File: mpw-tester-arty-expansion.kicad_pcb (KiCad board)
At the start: 4 copper layers, 53.3 x 61.5 mm, 138 parts, among them J1 USB4105-GF-A, J10 61300211121, J11 61300211121, J12 61300211121, J13 61300211121, J14 61300211121, J15 61300211121, J16 61300211121, J17 61300211121, J18 61300411121, J19 61300711121, J2 61300211121, J20 61300411121, J3 Arty_A7_SPI, J4 61300211121, J5 61300311121, J6 61300211121, J7 61300211121, J8 61300211121, J9 61300211121, Q1 DTC014TEBTL, U1 SN74LVC1G125DCKR, U2 FT232HQ, U3 SN74LVC1G125DCKR, U4 MAX811REUS+T, U5 NTS0102GT, U6 MCP4661-103E/ML, U7 Caravel_breakout_PCB, U8 W25Q32FVSS, U9 MIC2211-AAYML-TR, Y1 ABM8G-12.000MHZ-18-D2Y-T, Y2 ECS-2520MVLC-100-BN-TR

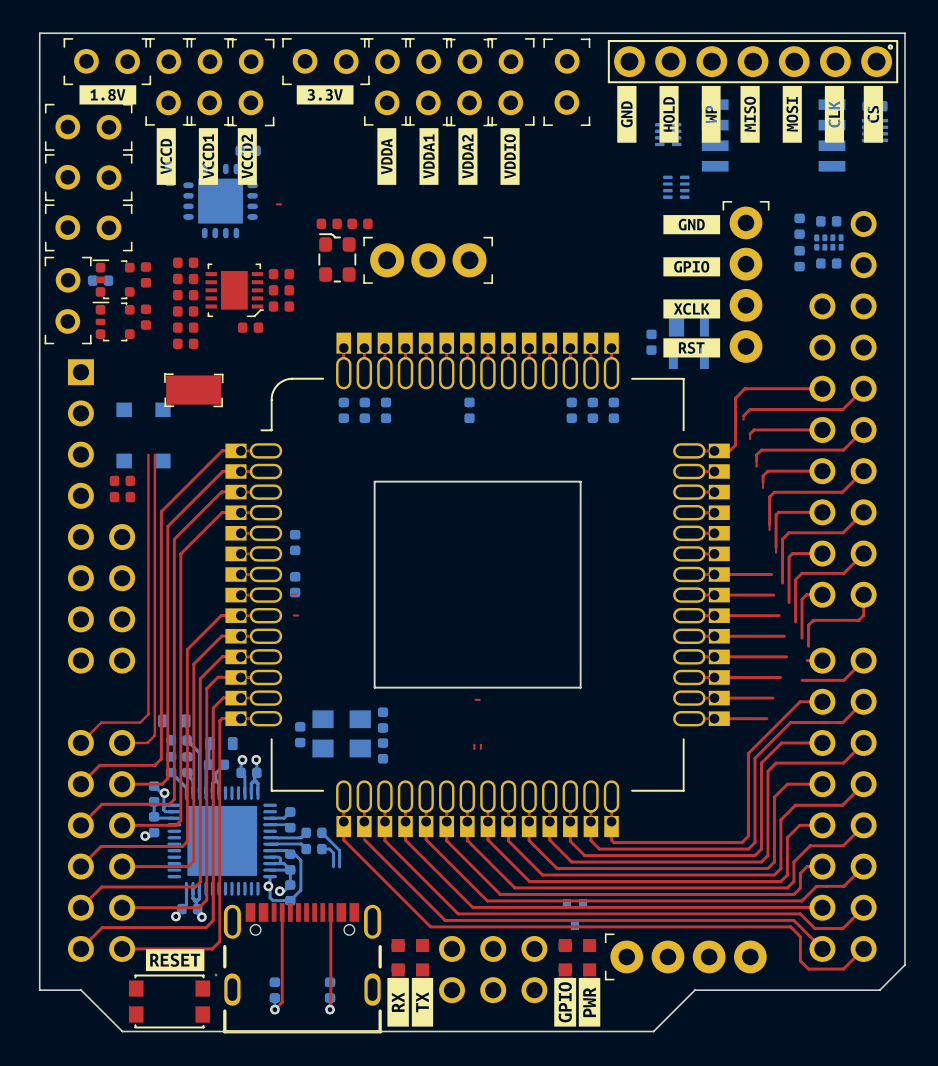
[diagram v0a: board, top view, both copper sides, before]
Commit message: Import changes to PCB, adjust placement
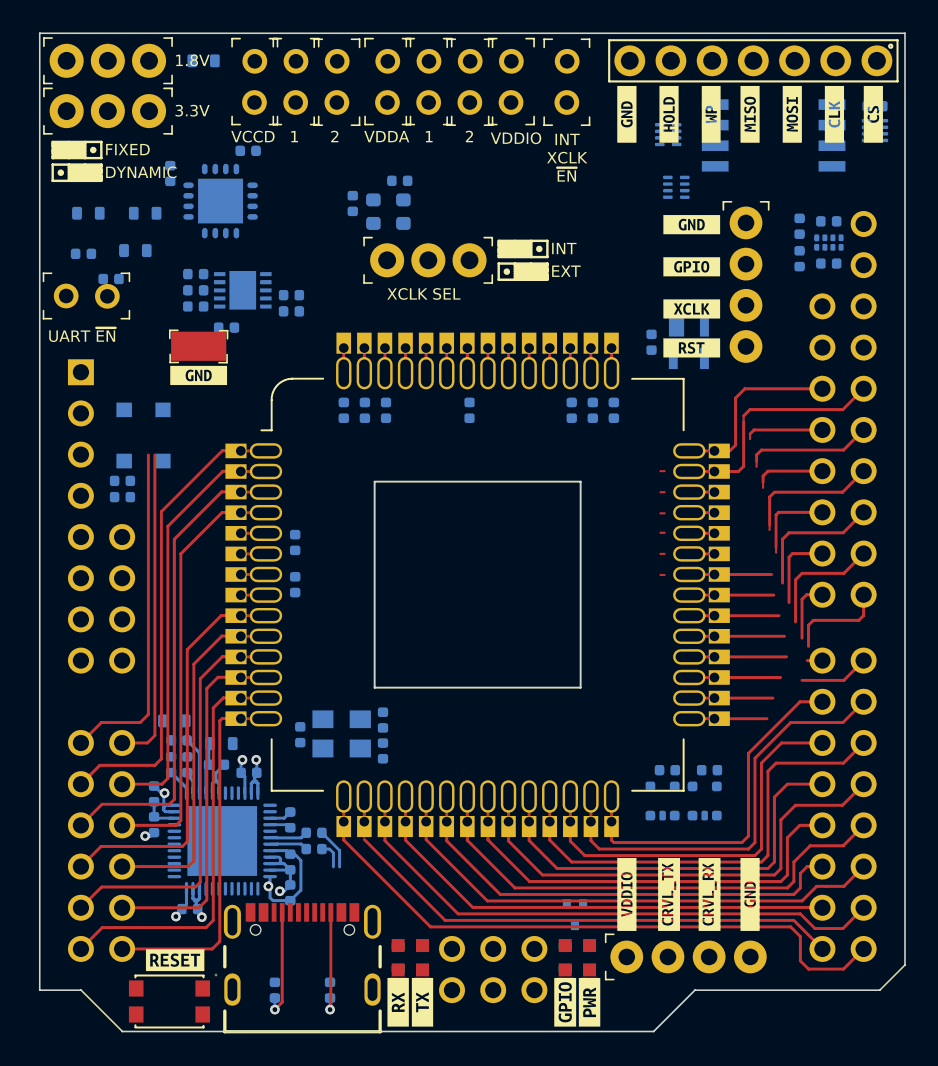
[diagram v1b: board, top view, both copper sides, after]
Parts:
- removed J13, J16, J17: 61300211121, antmicro-footprints:PinHeader_1x2_P2.54_Drill0.9mm
- removed kibuzzard-638FA122: G***, kibuzzard-638FA122
- removed kibuzzard-638FA139: G***, kibuzzard-638FA139
- removed kibuzzard-638FA13E: G***, kibuzzard-638FA13E
- removed kibuzzard-638FA141: G***, kibuzzard-638FA141
- removed kibuzzard-638FA14D: G***, kibuzzard-638FA14D
- removed kibuzzard-638FA15A: G***, kibuzzard-638FA15A
- removed kibuzzard-638FA169: G***, kibuzzard-638FA169
- removed kibuzzard-638FA16F: G***, kibuzzard-638FA16F
- removed kibuzzard-638FA174: G***, kibuzzard-638FA174
- added R26: R_10k_0603, antmicro-footprints:0603-res, B.Cu at (133.1, 67.7)
- added kibuzzard-638FA1CB: G***, kibuzzard-638FA1CB, F.Cu at (132.8, 87.1)
- added kibuzzard-639040B1: G***, kibuzzard-639040B1, F.Cu at (164.3, 119.1)
- added kibuzzard-639040B6: G***, kibuzzard-639040B6, F.Cu at (161.8, 119.1)
- added kibuzzard-639040BB: G***, kibuzzard-639040BB, F.Cu at (159.2, 119.1)
- added kibuzzard-639040CA: G***, kibuzzard-639040CA, F.Cu at (166.8, 119.1)
- C10, C18, C19, C3, C32, C33, C35, C36, C4, R11, R17, R21, U1, U3, U9, Y2: moved to B.Cu
- J14, J15: value 61300211121 -> 61300311121; footprint antmicro-footprints:PinHeader_1x2_P2.54_Drill0.9mm -> antmicro-footprints:PinHeader_1x3_P2.54_Drill1.1mm
- R22: value R_10k_0402 -> R_68k_0603; footprint antmicro-footprints:0402-res -> antmicro-footprints:0603-res; moved to B.Cu
- R23: value R_10k_0402 -> R_41k2_0603; footprint antmicro-footprints:0402-res -> antmicro-footprints:0603-res; moved to B.Cu
- R24: value R_10k_0402 -> R_15k_0603; footprint antmicro-footprints:0402-res -> antmicro-footprints:0603-res; moved to B.Cu
- R25: value R_10k_0402 -> R_34k_0402; moved to B.Cu
- moved U1 48.5 mm to (164.0, 113.3), turned to 180 degrees
- moved C10 46.3 mm to (164.3, 111.4), turned to 180 degrees
- moved U3 44.9 mm to (161.4, 113.3), turned to 180 degrees
- moved C18 42.6 mm to (161.7, 111.4), turned to 180 degrees
- moved NT9 28.8 mm to (161.4, 93.0), turned to 180 degrees
- moved NT11 22.9 mm to (161.4, 98.1), turned to 180 degrees
- moved NT12 22.7 mm to (161.4, 99.4), turned to 180 degrees
- moved NT8 19.5 mm to (161.4, 94.3), turned to 180 degrees
- moved NT7 17.3 mm to (161.4, 96.8), turned to 180 degrees
- moved NT10 16.2 mm to (161.4, 95.6), turned to 180 degrees
- moved J15 10.6 mm to (124.7, 67.7), turned to 0 degrees
- moved R25 8.40 mm to (125.7, 79.6)
- moved R23 6.73 mm to (126.0, 77.1)
- moved C35 6.52 mm to (138.5, 83.2), turned to 0 degrees
- moved C36 6.52 mm to (138.5, 82.2), turned to 0 degrees
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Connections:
- net /ADJ1 renamed /P0W
- net /ADJ2 renamed /P1W
- C23 pad 1: /5V0_SEL -> /5V0
- C32 pad 1: /5V0_SEL -> /5V0
- C35 pad 1: /VOUT1 -> +3V3
- C36 pad 1: /VOUT2 -> +1V8
- J14 pad 1: /P1A -> /P0B
- J14 pad 2: /P1B -> /P0A
- J15 pad 1: /P0A -> /P1B
- J15 pad 2: /P0B -> /P1A
- R14 pad 2: /5V0_SEL -> /5V0
- R15 pad 1: /5V0_SEL -> /5V0
- R17 pad 1: /5V0_SEL -> /5V0
- R19 pad 1: /5V0_SEL -> /5V0
- R21 pad 1: /5V0_SEL -> /5V0
- R22 pad 1: /P1A -> /P0A
- R22 pad 2: /VOUT2 -> +3V3
- R23 pad 2: /P1B -> /P0B
- R24 pad 1: /P0A -> /P1A
- R24 pad 2: /VOUT1 -> +1V8
- R25 pad 2: /P0B -> /P1B
- U5 pad 7: /5V0_SEL -> /5V0
- U6 pad 15: /5V0_SEL -> /5V0
- U9 pad 1: /5V0_SEL -> /5V0
- U9 pad 10: /VOUT1 -> +3V3
- U9 pad 9: /VOUT2 -> +1V8
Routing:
- net /CRVL_IO1: track 1.55 -> 6.25 mm
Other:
- board text added: "1"
- board text added: "1.8V"
- board text added: "2"
- board text added: "3.3V"
- board text added: "DYNAMIC"
- board text added: "EXT"
- board text added: "FIXED"
- board text added: "INT"
- board text added: "INT XCLK ~{EN}"
- board text added: "UART ~{EN}"
- board text added: "VCCD"
- board text added: "VDDA"
- board text added: "VDDIO"
- board text added: "XCLK SEL"

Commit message: Import changes to PCB. Adjust placement. Partial layout
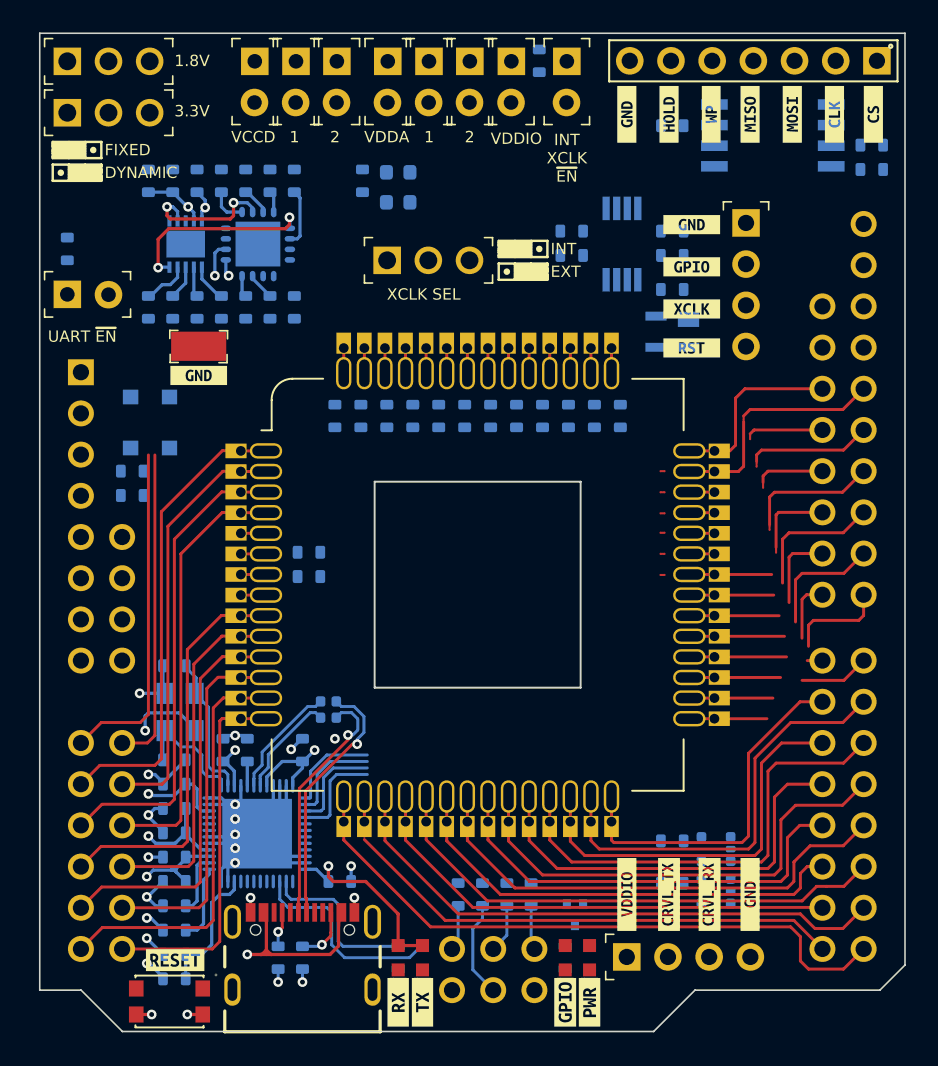
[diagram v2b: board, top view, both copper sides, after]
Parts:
- removed C13: C_100n_0402, antmicro-footprints:0402-cap
- added C37: C_100n_0603, antmicro-footprints:0603-cap, B.Cu at (137.2, 82.9)
- added R27: R_4k7_0603, antmicro-footprints:0603-res, B.Cu at (155.8, 78.2)
- added R28: R_10k_0603, antmicro-footprints:0603-res, B.Cu at (162.0, 71.7)
- added R29: R_0R_0603, antmicro-footprints:0603-res, B.Cu at (135.7, 82.9)
- added R30: R_10k_0603, antmicro-footprints:0603-res, B.Cu at (131.2, 82.9)
- added R31: R_4k7_0603, antmicro-footprints:0603-res, B.Cu at (155.8, 79.7)
- added R32: R_10k_0603, antmicro-footprints:0603-res, B.Cu at (174.3, 72.9)
- added R33: R_10k_0603, antmicro-footprints:0603-res, B.Cu at (132.7, 82.9)
- added R34: R_10k_0603, antmicro-footprints:0603-res, B.Cu at (146.0, 89.6)
- C1, C22, C23, C24, C26, C27, C28, C29, C30, C31: value C_100n_0402 -> C_1u_0603; footprint antmicro-footprints:0402-cap -> antmicro-footprints:0603-cap
- C10, C11, C14, C15, C16, C18, C19, C20, C21, C25, C33, C34, C5, C7, C8: value C_100n_0402 -> C_100n_0603; footprint antmicro-footprints:0402-cap -> antmicro-footprints:0603-cap
- C17: value C_10n_0402 -> C_10n_0603; footprint antmicro-footprints:0402-cap -> antmicro-footprints:0603-cap
- C3, C32, C35, C36: value C_1u_0402 -> C_1u_0603; footprint antmicro-footprints:0402-cap -> antmicro-footprints:0603-cap
- C4: value C_1u_0402 -> C_100n_0603; footprint antmicro-footprints:0402-cap -> antmicro-footprints:0603-cap
- C6, C9: value C_18p_0402 -> C_18p_0603; footprint antmicro-footprints:0402-cap -> antmicro-footprints:0603-cap
- R1, R17, R21, R6: value R_10k_0402 -> R_10k_0603; footprint antmicro-footprints:0402-res -> antmicro-footprints:0603-res
- R11, R14: value R_10k_0402 -> R_0R_0603; footprint antmicro-footprints:0402-res -> antmicro-footprints:0603-res
- R15: value R_4k7_0402 -> R_0R_0603; footprint antmicro-footprints:0402-res -> antmicro-footprints:0603-res
- R16, R20: value 4x10k_0201_array -> R_10k_0603; footprint antmicro-footprints:EXB18V -> antmicro-footprints:0603-res
- R18: value R_0R_0402 -> R_10k_0603; footprint antmicro-footprints:0402-res -> antmicro-footprints:0603-res
- R19: value R_4k7_0402 -> R_10k_0603; footprint antmicro-footprints:0402-res -> antmicro-footprints:0603-res
- R2, R3: value R_5k1_0402 -> R_5k1_0603; footprint antmicro-footprints:0402-res -> antmicro-footprints:0603-res
- R25: value R_34k_0402 -> R_34k_0603; footprint antmicro-footprints:0402-res -> antmicro-footprints:0603-res
- R7: value R_12k_0402 -> R_12k_1%_0603; footprint antmicro-footprints:0402-res -> antmicro-footprints:0603-res
- R8: value 4x0R_0201_array -> R_0R_0603; footprint antmicro-footprints:EXB18V -> antmicro-footprints:0603-res
- U5: value NTS0102GT -> NTS0102DP; footprint antmicro-footprints:PSON50P100X195X50-8N -> antmicro-footprints:TSSOP-8_W3mm
- moved R14 49.7 mm to (153.3, 119.1)
- moved R8 45.6 mm to (148.8, 119.1), turned to 90 degrees
- moved R15 45.6 mm to (150.3, 119.1), turned to 90 degrees
- moved R11 43.6 mm to (151.8, 119.1), turned to 90 degrees
- moved C23 28.8 mm to (144.4, 89.6), turned to -90 degrees
- moved R20 25.4 mm to (138.7, 82.9), turned to 90 degrees
- moved R18 24.4 mm to (154.0, 89.6), turned to 90 degrees
- moved C1 22.2 mm to (128.7, 94.5), turned to 0 degrees
- moved R19 21.4 mm to (150.8, 89.6)
- moved R16 21.1 mm to (153.8, 67.7), turned to -90 degrees
- moved R21 20.9 mm to (152.4, 89.6), turned to 90 degrees
- moved C4 18.0 mm to (131.3, 112.3), turned to 180 degrees
- moved R17 16.9 mm to (147.6, 89.6), turned to 90 degrees
- moved C24 14.5 mm to (158.8, 89.6)
- moved C9 13.3 mm to (131.3, 105.0), turned to 180 degrees
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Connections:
- net Net-(C33-Pad1) renamed /BYP
- C1 pad 1: /FTDI_3V3 -> /3V3_ARTY
- C23 pad 1: /5V0 -> /VDDA2
- C24 pad 1: /VDDA2 -> /VCCD1
- C25 pad 1: /VCCD1 -> /5V0
- C3 pad 1: /3V3_ARTY -> /5V0_ARTY
- C4 pad 1: /5V0_ARTY -> /FTDI_3V3
- J12 pad 1: /VCCD2 -> +1V8
- J12 pad 2: +1V8 -> /VCCD2
- J4 pad 1: Net-(J4-Pad1) -> /XCLK_EN
- J5 pad 1: /ARTY_XCLK -> /XCLK_10MHz
- J5 pad 3: /XCLK_10MHz -> /ARTY_XCLK
- J9 pad 1: /VDDA2 -> +3V3
- J9 pad 2: +3V3 -> /VDDA2
- R11 pad 1: Net-(J4-Pad1) -> /ARTY_MEM_SCK
- R11 pad 2: +3V3 -> /MEM.SCK
- R14 pad 1: Net-(R14-Pad1) -> /ARTY_MEM_MOSI
- R14 pad 2: /5V0 -> /MEM.SI
- R15 pad 1: /5V0 -> /ARTY_MEM_MISO
- R15 pad 2: /ARTY_SDA -> /MEM.SO
- R16 pad 1: unconnected-(R16-Pad1) -> /XCLK_EN
- R16 pad 2: /MEM.SI -> +3V3
- R17 pad 1: /5V0 -> +3V3
- R17 pad 2: /EN_VOUT2 -> /MEM.~{CS}
- R18 pad 1: AGND -> +3V3
- R18 pad 2: Net-(R18-Pad2) -> /MEM.SCK
- R19 pad 1: /5V0 -> +3V3
- R19 pad 2: /ARTY_SCL -> /MEM.SI
- R20 pad 1: unconnected-(R20-Pad1) -> /5V0
- R20 pad 2: /MEM.~{WP} -> /~{WP}
- R21 pad 1: /5V0 -> +3V3
- R21 pad 2: /EN_VOUT1 -> /MEM.SO
- R6 pad 1: /FTDI_RESET -> /FTDI_3V3
- R6 pad 2: /FTDI_3V3 -> /FTDI_RESET
- R8 pad 1: /ARTY_MEM_MISO -> /ARTY_MEM_CS
- R8 pad 2: /ARTY_MEM_MOSI -> /MEM.~{CS}
- U6 pad 12: Net-(R14-Pad1) -> /~{WP}
- U6 pad 16: Net-(R18-Pad2) -> /HVC
- Y2 pad 1: Net-(J4-Pad1) -> /XCLK_EN
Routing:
- net AGND: track 23.0 -> 74.4 mm, vias 4 -> 23
- net VBUS: track 3.15 -> 30.3 mm, vias 0 -> 2
- net /FTDI_3V3: track 18.8 -> 33.5 mm, vias 4 -> 6
- net /USB_DP: track 1.67 -> 15.7 mm, vias 0 -> 1
- net /USB_DN: track 2.55 -> 16.4 mm, vias 0 -> 1
- net /~{TX_LED}: track 0.00 -> 12.9 mm
- net /P0W: track 0.00 -> 12.1 mm, vias 0 -> 2
- net /~{RX_LED}: track 0.00 -> 10.4 mm
- net /XOUT: track 0.00 -> 8.93 mm
- net /P1W: track 0.00 -> 8.52 mm, vias 0 -> 2
- net /XIN: track 0.00 -> 7.61 mm
- net /USB_CS1: track 0.00 -> 6.18 mm
- net /USB_SI: track 0.00 -> 6.06 mm
- net /ARTY_MEM_MISO: track 0.00 -> 5.97 mm
- net /FTDI_RESET: track 2.22 -> 8.18 mm
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- added copper zone on In2.Cu, net /FTDI_3V3
- added copper zone on In1.Cu, net AGND
- added copper zone on In2.Cu, net AGND

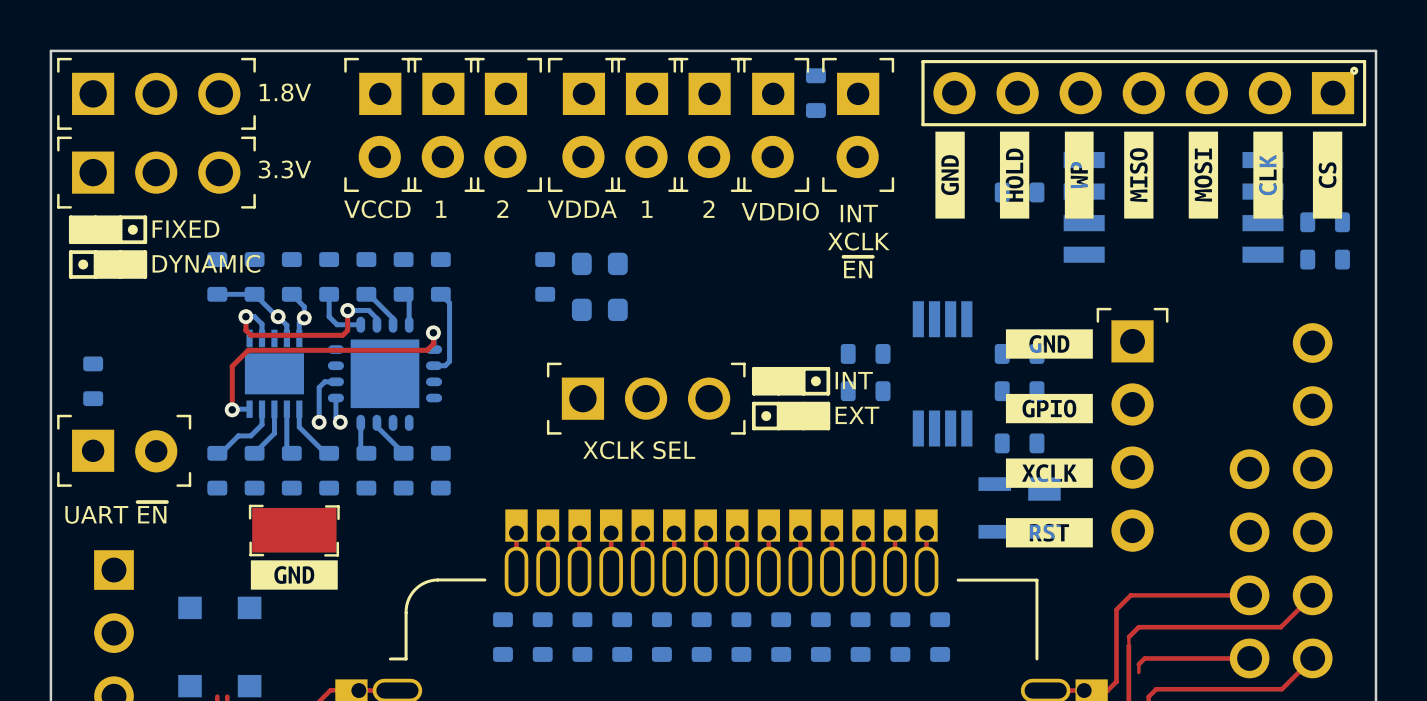
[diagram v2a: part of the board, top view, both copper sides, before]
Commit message: Improve placement of the pin headers
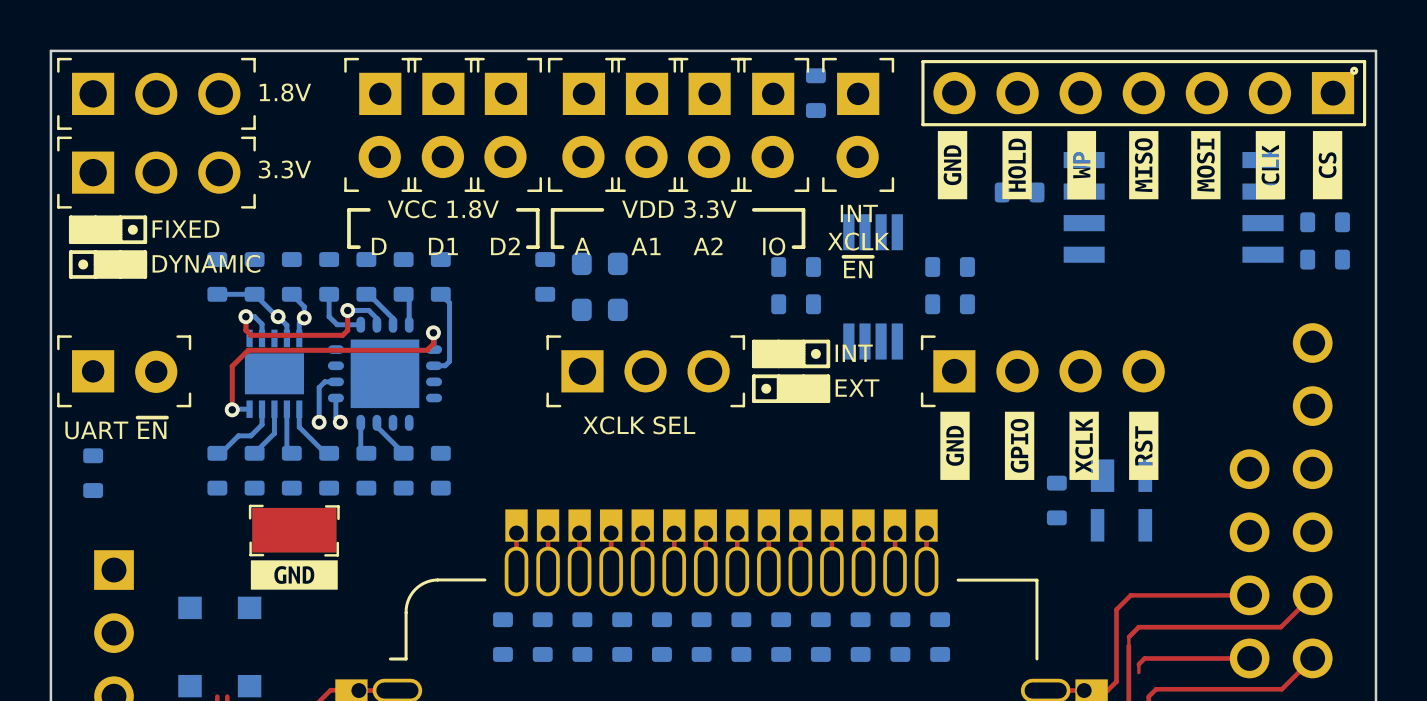
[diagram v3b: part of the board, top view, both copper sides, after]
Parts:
- removed kibuzzard-638FA1B0: G***, kibuzzard-638FA1B0
- removed kibuzzard-638FA1BB: G***, kibuzzard-638FA1BB
- removed kibuzzard-638FA1C5: G***, kibuzzard-638FA1C5
- removed the kibuzzard-638FA1CB at (163.2, 77.8)
- removed the kibuzzard-638FA1CB at (159.2, 71.0)
- removed kibuzzard-638FA1F4: G***, kibuzzard-638FA1F4
- removed kibuzzard-638FA1F9: G***, kibuzzard-638FA1F9
- removed kibuzzard-638FA208: G***, kibuzzard-638FA208
- removed kibuzzard-638FA20C: G***, kibuzzard-638FA20C
- removed kibuzzard-638FA213: G***, kibuzzard-638FA213
- removed kibuzzard-638FA216: G***, kibuzzard-638FA216
- added kibuzzard-639091D1: G***, kibuzzard-639091D1, F.Cu at (162.0, 81.9)
- added kibuzzard-639091D4: G***, kibuzzard-639091D4, F.Cu at (159.4, 81.9)
- added kibuzzard-639091D8: G***, kibuzzard-639091D8, F.Cu at (164.6, 81.9)
- added kibuzzard-639091DC: G***, kibuzzard-639091DC, F.Cu at (167.0, 81.9)
- added kibuzzard-63909224: G***, kibuzzard-63909224, F.Cu at (159.3, 70.6)
- added kibuzzard-63909228: G***, kibuzzard-63909228, F.Cu at (167.0, 70.6)
- added kibuzzard-63909232: G***, kibuzzard-63909232, F.Cu at (169.5, 70.6)
- added kibuzzard-63909236: G***, kibuzzard-63909236, F.Cu at (161.9, 70.6)
- added kibuzzard-6390923A: G***, kibuzzard-6390923A, F.Cu at (164.5, 70.6)
- added kibuzzard-6390923D: G***, kibuzzard-6390923D, F.Cu at (172.1, 70.6)
- added kibuzzard-63909242: G***, kibuzzard-63909242, F.Cu at (174.4, 70.6)
- moved J20 7.27 mm to (159.4, 78.9), turned to 0 degrees
- moved C21 4.48 mm to (159.2, 74.7)
- moved C25 4.48 mm to (159.2, 76.2)
- moved R27 4.48 mm to (153.0, 74.7)
- moved R31 4.48 mm to (153.0, 76.2)
- moved U5 4.48 mm to (156.1, 75.5)
- moved U4 4.11 mm to (166.1, 84.1), turned to 0 degrees
- moved R1 3.70 mm to (124.7, 83.0), turned to -90 degrees
- moved J2 3.20 mm to (124.7, 78.9)
- moved C20 2.75 mm to (163.5, 84.1), turned to 90 degrees
- moved J5 1.10 mm to (144.4, 78.9)
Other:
- board text added: "A"
- board text added: "A1"
- board text added: "A2"
- board text added: "D"
- board text added: "D1"
- board text added: "D2"
- board text added: "IO"
- board text added: "VCC 1.8V"
- board text added: "VDD 3.3V"
- board text removed: "1"
- board text removed: "2"
- board text removed: "VCCD"
- board text removed: "VDDA"
- board text removed: "VDDIO"
